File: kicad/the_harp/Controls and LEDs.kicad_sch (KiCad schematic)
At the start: 19 parts, among them J408 OLED 0.91 128x32, SW101 100-DP6, SW102 100-DP6, SW103 100-DP6

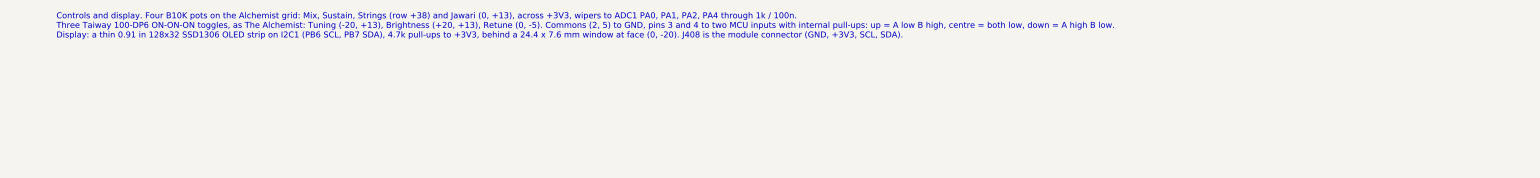
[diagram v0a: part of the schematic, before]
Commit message: Option 1: OLED at (0, -5), Retune toggle at (0, -24), re-placed board
Face: the OLED window moves up into the middle of the face under the
Jawari knob, the Retune toggle moves down to (0, -24) (design brief,
decision 16). The module is mounted turned round, pads at its right end;
the firmware flips the image.

Board: with the toggle out of the middle the H750 moves up to (0, -7),
under the screen. Codec beside it next to the SAI pins (11-16 mm), ADC
driver below the codec (left ADC pair 17-19 mm), input buffers and flash
on the right next to IN, output stages and VCOM buffers between the pot
rows, J408 at the module's right end (22, -3.5). Bottom side as before,
relay now under U201 at (0, -8). Placer now works on a 0.5 mm grid and
prefers spots that line up with the rest of the group and share its
orientation. Checked from the board file: no overlaps either side,
nothing on through-holes, nothing tall under the module.

Face cut-out and OLED drawings, placement drawing, PCB plan, brief,
firmware requirements, design report and schematic notes updated.

Co-Authored-By: Claude Opus 5.5 <noreply@anthropic.com>
Claude-Session: https://claude.ai/code/session_016hDejPHPgG8auBLMyByYZK
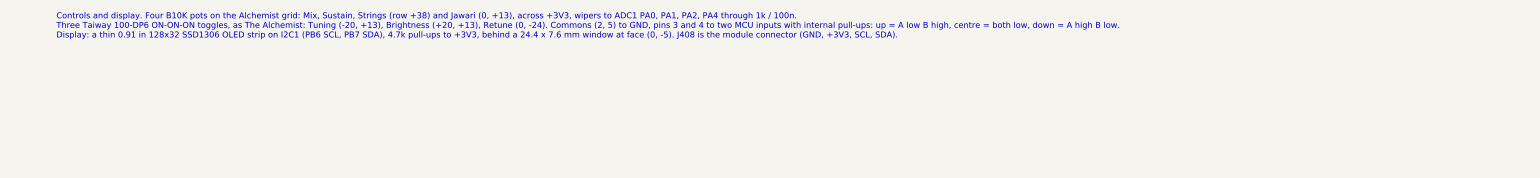
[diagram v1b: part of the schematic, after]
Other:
- note added: "Controls and display. Four B10K pots on the Alchemist grid: Mix, Sustain, Strings (row +38) and Jawari (0, +13), across +3V3, wipers to ADC1 PA0, PA1, PA2, PA4 through 1k / 100n. Three Taiway 100-DP6 ON-ON-ON toggles, as The Alchemist: Tuning (-20, +13), Brightness (+20, +13), Retune (0, -24). Commons (2, 5) to GND, pins 3 and 4 to two MCU inputs with internal pull-ups: up = A low B high, centre 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"
- note removed: "Controls and display. Four B10K pots on the Alchemist grid: Mix, Sustain, Strings (row +38) and Jawari (0, +13), across +3V3, wipers to ADC1 PA0, PA1, PA2, PA4 through 1k / 100n. Three Taiway 100-DP6 ON-ON-ON toggles, as The Alchemist: Tuning (-20, +13), Brightness (+20, +13), Retune (0, -5). Commons (2, 5) to GND, pins 3 and 4 to two MCU inputs with internal pull-ups: up = A low B high, centre =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"
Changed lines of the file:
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@@
 		(at 228.6 134.62)
 	)
-	(text "Controls and display. Four B10K pots on the Alchemist grid: Mix, Sustain, Strings (row +38) and Jawari (0, +13), across +3V3, wipers to ADC1 PA0, PA1, PA2, PA4 through 1k / 100n.\nThree Taiway 100-DP6 ON-ON-ON toggles, as The Alchemist: Tuning (-20, +13), Brightness (+20, +13), Retune (0, -5). Commons (2, 5) to GND, pins 3 and 4 to two MCU inputs with internal pull-ups: up = A low B high, centre = both low, down = A high B low.\nDisplay: a thin 0.91 in 128x32 SSD1306 OLED strip on I2C1 (PB6 SCL, PB7 SDA), 4.7k pull-ups to +3V3, behind a 24.4 x 7.6 mm window at face (0, -20). J408 is the module connector (GND, +3V3, SCL, SDA)."
+	(text "Controls and display. Four B10K pots on the Alchemist grid: Mix, Sustain, Strings (row +38) and Jawari (0, +13), across +3V3, wipers to ADC1 PA0, PA1, PA2, PA4 through 1k / 100n.\nThree Taiway 100-DP6 ON-ON-ON toggles, as The Alchemist: Tuning (-20, +13), Brightness (+20, +13), Retune (0, -24). Commons (2, 5) to GND, pins 3 and 4 to two MCU inputs with internal pull-ups: up = A low B high, centre = both low, down = A high B low.\nDisplay: a thin 0.91 in 128x32 SSD1306 OLED strip on I2C1 (PB6 SCL, PB7 SDA), 4.7k pull-ups to +3V3, behind a 24.4 x 7.6 mm window at face (0, -5). J408 is the module connector (GND, +3V3, SCL, SDA)."
 		(exclude_from_sim no)
 		(at 20.32 15.24 0)
